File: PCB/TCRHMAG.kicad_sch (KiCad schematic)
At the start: 4 parts, among them J1 CONN_LED, J2 CONN_THERM, J3 CONN_OLED, SW1 PWR_SW

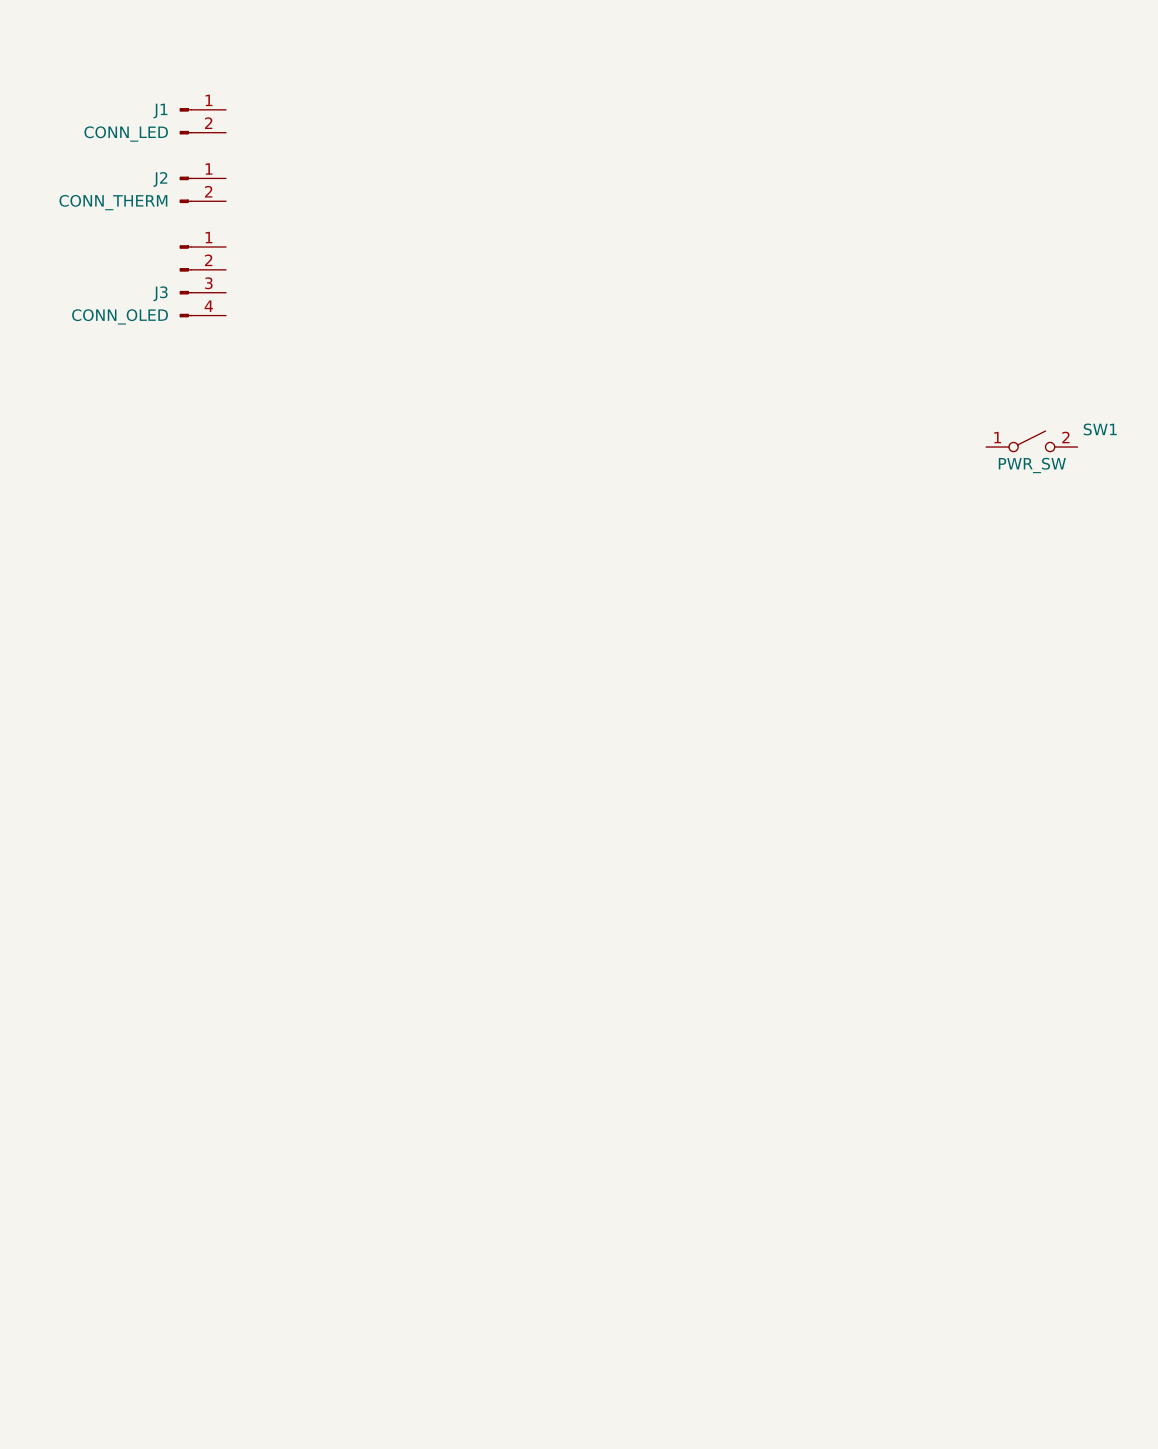
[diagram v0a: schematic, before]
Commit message: PCB Components Chosen
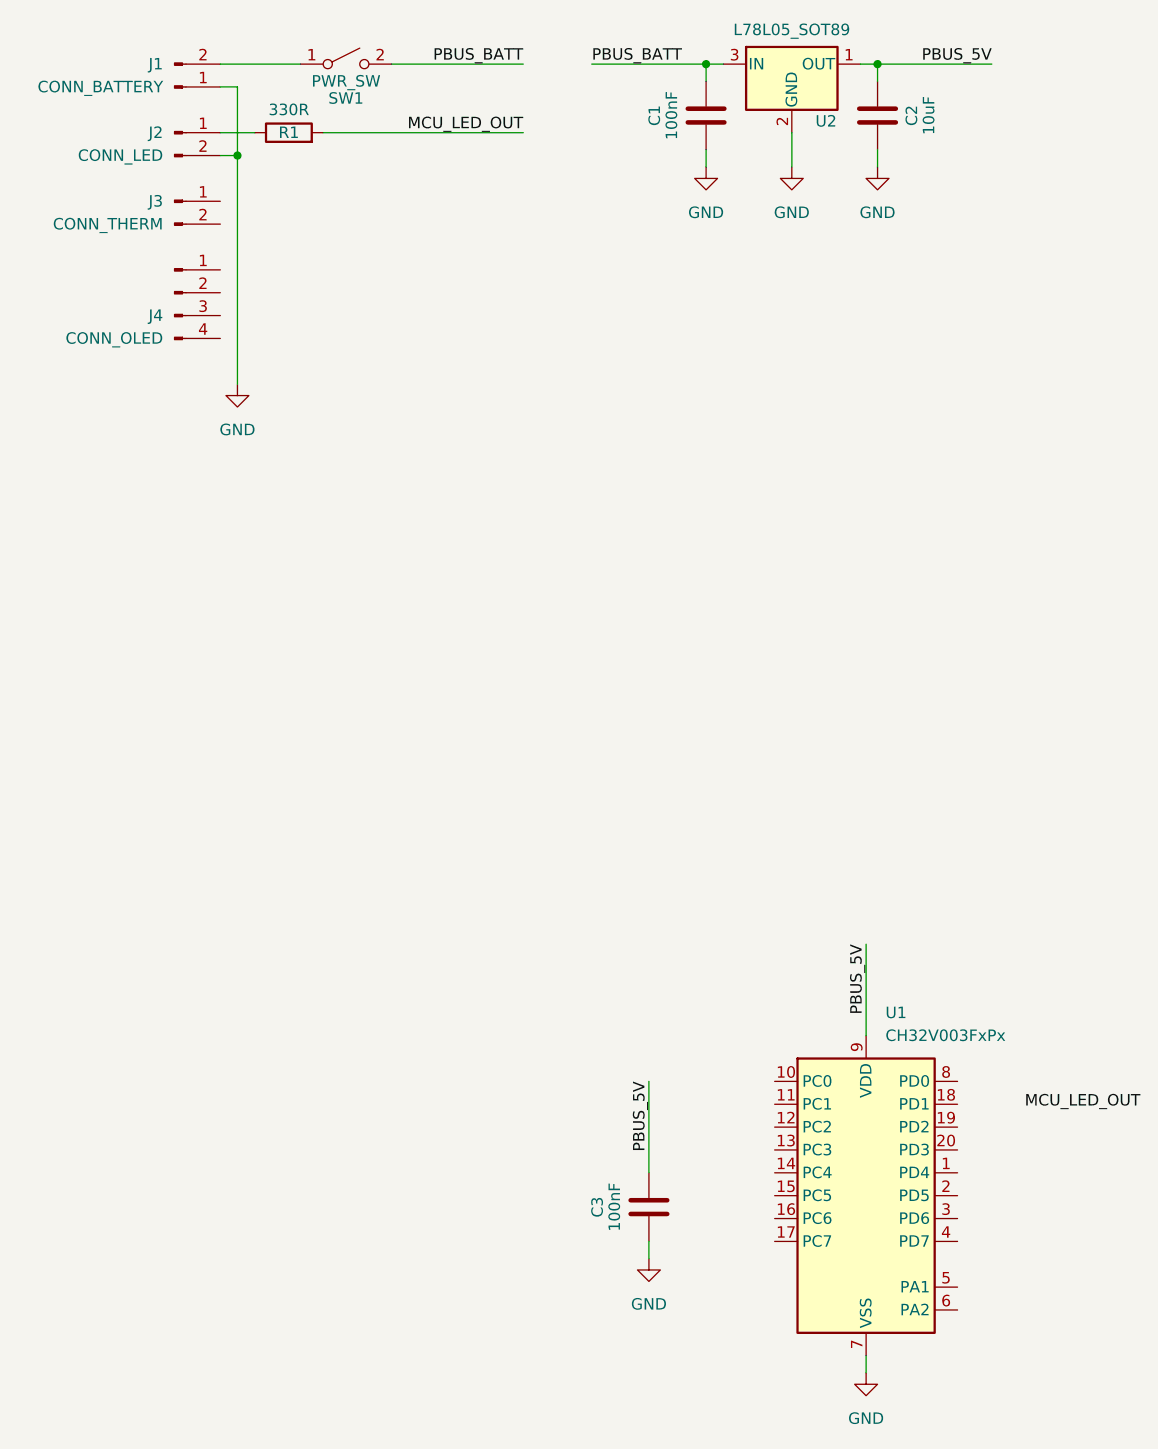
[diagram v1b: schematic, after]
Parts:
- added C1, C3: 100nF, Capacitor_SMD:C_0603_1608Metric, symbol Device:C
- added C2: 10uF, Capacitor_SMD:C_0603_1608Metric, symbol Device:C
- added J1: CONN_BATTERY, TCRHMAG:Power_Conn, symbol Connector:Conn_01x02_Pin
- added R1: 330R, Resistor_SMD:R_0603_1608Metric, symbol Device:R
- added U1: CH32V003FxPx, Package_SO:TSSOP-20_4.4x6.5mm_P0.65mm, symbol MCU_WCH_RiscV:CH32V003FxPx
- added U2: L78L05_SOT89, Package_TO_SOT_SMD:SOT-89-3, symbol Regulator_Linear:L78L05_SOT89
- renumbered J1 to J2, J2 to J3, J3 to J4
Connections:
- net at SW1.1 (A): now also J1.2 (Pin_2)
- net PBUS_BATT: now reaches SW1.2 (B)
- net PBUS_BATT: now also C1.1, U2.3 (IN)
- net at J2.1 (Pin_1): now also R1.1
- net GND: now reaches J2.2 (Pin_2)
- net GND: now also C1.2, C2.2, C3.2, J1.1 (Pin_1), U1.7 (VSS), U2.2 (GND)
- new net MCU_LED_OUT: R1.2
- new net PBUS_5V: C2.1, C3.1, U1.9 (VDD), U2.1 (OUT)
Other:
- company: (none) -> ADBeta
- title: (none) -> TCRHMAG
- moved on the sheet: J2, J3, J4, SW1

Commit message: Added Current Sense to circuit
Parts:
- added C103: 1uF, Capacitor_SMD:C_0603_1608Metric, symbol Device:C
- added C201, C301, C302: 100nF, Capacitor_SMD:C_0603_1608Metric, symbol Device:C_Small
- added J5: CONN_HEATER, TCRHMAG:Power_Conn, symbol Connector:Conn_01x02_Pin
- added MCU_OPAMP_CONFIG_1, MCU_OPAMP_CONFIG_2: ~, symbol TCRHMAG:VIRTUAL_OPAMP
- added Q301: Si4116DY, Package_SO:SOIC-8_3.9x4.9mm_P1.27mm, symbol Project_Sym:Si4116DY
- added R102: 4K7, Resistor_SMD:R_0603_1608Metric, symbol Device:R
- added R103: 10R, Resistor_SMD:R_0603_1608Metric, symbol Device:R
- added R104, R202, R303: 33K, Resistor_SMD:R_0603_1608Metric, symbol Device:R
- added R201, R204: 2K2, Resistor_SMD:R_0603_1608Metric, symbol Device:R
- added R203: 68K, Resistor_SMD:R_0603_1608Metric, symbol Device:R
- added R301, R302: 0R1, Resistor_SMD:R_2512_6332Metric_Pad1.40x3.35mm_HandSolder, symbol Device:R
- renumbered C1 to C101, C2 to C102, C3 to C104, R1 to R101, SW1 to SW101, U2 to U101, U1 to U102
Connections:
- net GND: now also J3.2 (Pin_2), C103.1, C201.2, C301.2, C302.2, R104.1, R201.1, R204.1, R301.2, R302.2
- net PBUS_5V: now also R102.2, R203.1
- net PBUS_BATT: now also J5.2 (Pin_2)
- net MCU_OPAMP_OUT: now reaches U102.1 (PD4)
- net MCU_OPAMP_OUT: now also C201.1, MCU_OPAMP_CONFIG_1.3, MCU_OPAMP_CONFIG_2.3, R202.2
- net MCU_PWM_OUT: now reaches U102.10 (PC0)
- net MCU_PWM_OUT: now also R103.1
- net MCU_SDA: now reaches U102.11 (PC1)
- net MCU_SCL: now reaches U102.12 (PC2)
- net MCU_OPAMP_CH2+: now reaches U102.4 (PD7)
- net MCU_OPAMP_CH2+: now also MCU_OPAMP_CONFIG_2.1 (+), R203.2, R204.2
- net MCU_OPAMP_CH1-: now reaches U102.5 (PA1)
- net MCU_OPAMP_CH1-: now also MCU_OPAMP_CONFIG_1.2 (-), MCU_OPAMP_CONFIG_2.2 (-), R201.2, R202.1
- net MCU_OPAMP_CH1+: now reaches U102.6 (PA2)
- net MCU_OPAMP_CH1+: now also C302.1, MCU_OPAMP_CONFIG_1.1 (+), R303.1
- net MCU_SWIO: now reaches U102.8 (PD0)
- net MCU_THERM_IN: now reaches J3.1 (Pin_1)
- net MCU_THERM_IN: now also C103.2, R102.1
- new net: Q301.4 (G), R103.2, R104.2
- new net: J5.1 (Pin_1), Q301.5 (D), Q301.6 (D), Q301.7 (D), Q301.8 (D)
- new net CSENSE_FILL: C301.1, Q301.1 (S), Q301.2 (S), Q301.3 (S), R301.1, R302.1, R303.2
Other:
- note added: "Current Sense Amplification Gain = (1 + (33K / 2K2)) = 16.0"
- note added: "Maximum Measurable Current = Power Dissipation @ 5A(Nom) ="
- note added: "OpAmp Calibration Reference (VCC / 32) * 16x gain = VCC/2"
- moved on the sheet: C104, SW101, U102

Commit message: Added High Current and MCU to PCB
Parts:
- added R101: 33K, Resistor_SMD:R_0603_1608Metric, symbol Device:R
- added R102: 8K2, Resistor_SMD:R_0603_1608Metric, symbol Device:R
- Q301: symbol Project_Sym:Si4116DY -> TCRHMAG:Si4116DY
- R301, R302: value 0R1 -> 0R075
- renumbered R101 to R103, R102 to R104, R103 to R105, R104 to R106
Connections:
- net GND: now also R102.1
- net PBUS_BATT: now also J5.1 (Pin_1), R101.2; no longer J5.2 (Pin_2)
- net HEATER_FILL: now reaches Q301.5 (D), Q301.6 (D), Q301.7 (D), Q301.8 (D)
- net HEATER_FILL: now also J5.2 (Pin_2); no longer J5.1 (Pin_1)
- net BATTERY_FILL: now reaches J1.2 (Pin_2), SW101.1 (A)
- new net MCU_BATT_VSENS: R101.1, R102.2
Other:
- note added: "Maximum Measurable Current = 8.33A Power Dissipation @ 5A(Nom) = 0.94W Current per ADC Count = 2.03mA"
- note removed: "Maximum Measurable Current = Power Dissipation @ 5A(Nom) ="
- moved on the sheet: C101, C102, C104, U101
